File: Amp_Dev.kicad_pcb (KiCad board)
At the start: 2 copper layers, 100 x 100 mm, 512 parts, among them J1 SMA, J10 SMA, J11 CONN_01X02, J12 TEST_1P, J13 SMA, J14 CONN_01X02, J15 CONN_01X03, J16 TEST_1P, J17 TEST_1P, J18 TEST_1P, J2 SMA, J20 SMA, J21 SMA, J22 SMA, J3 TEST_1P, J4 TEST_1P, J5 CONN_01X03, J6 TEST_1P, J7 CONN_01X03, J8 TEST_1P, J9 TEST_1P, Q1 DMN2075U, U1 MML09211H, U2 RF6886, U3 LMV358, U4 SN74LVC1G17, U5 TLV702, U6 LTC2644, U7 RT9183

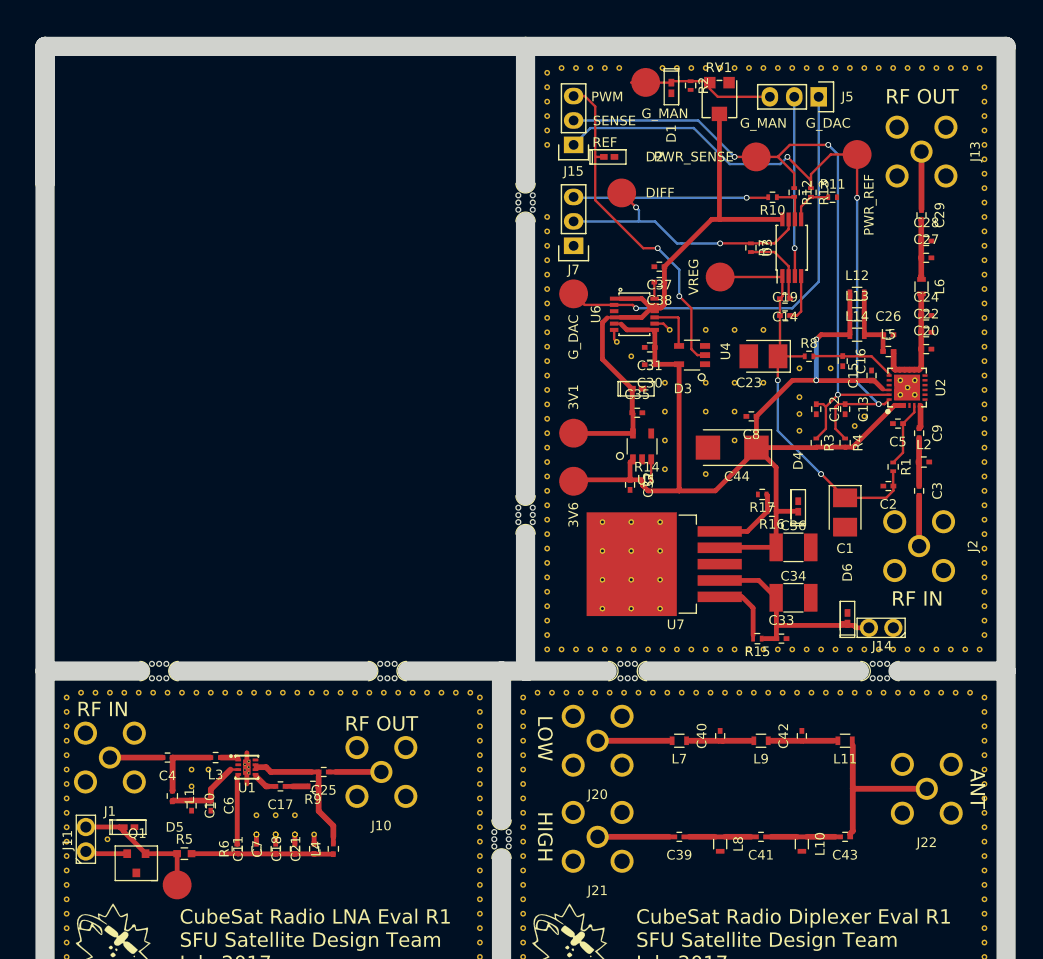
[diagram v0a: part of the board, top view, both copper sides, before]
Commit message: placed reference designators. resolves #9
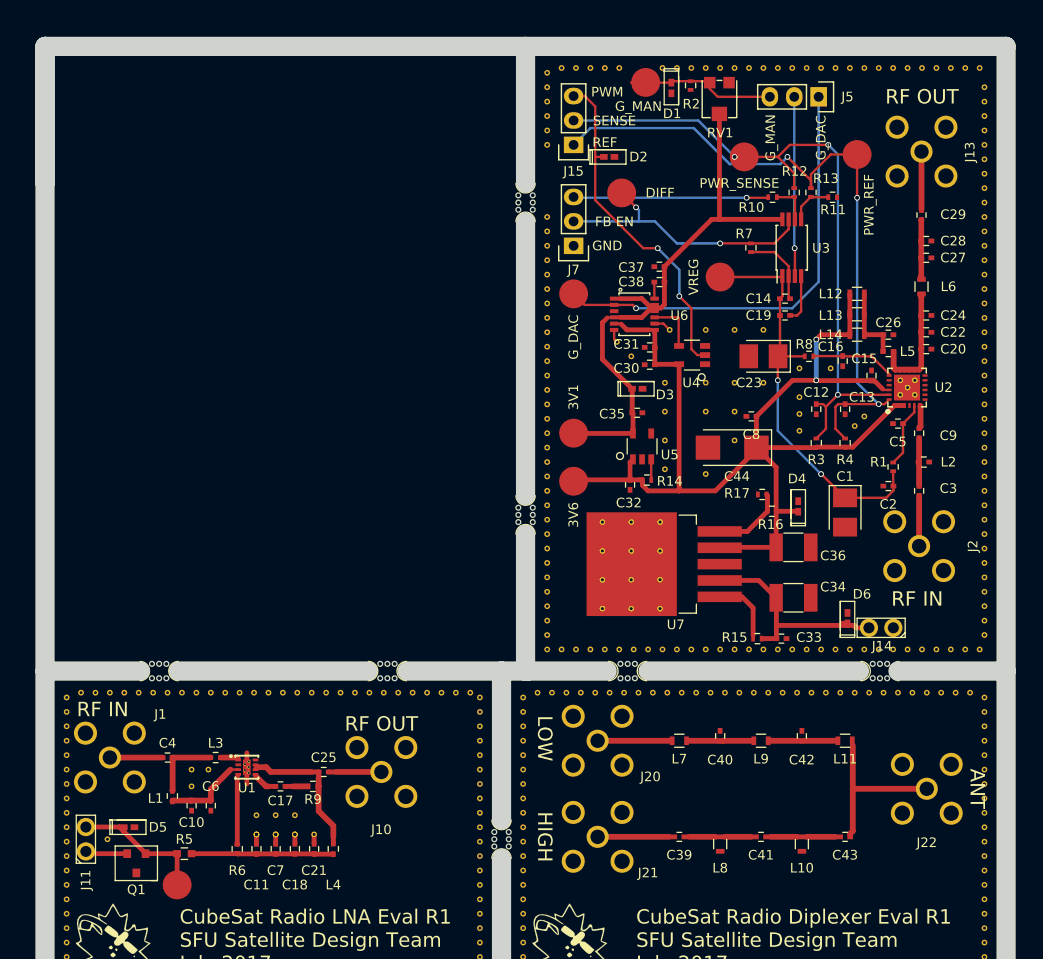
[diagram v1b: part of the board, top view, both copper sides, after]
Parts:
- moved J8 1.25 mm to (172.8, 61.5)
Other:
- board text added: "FB EN"
- board text added: "GND"

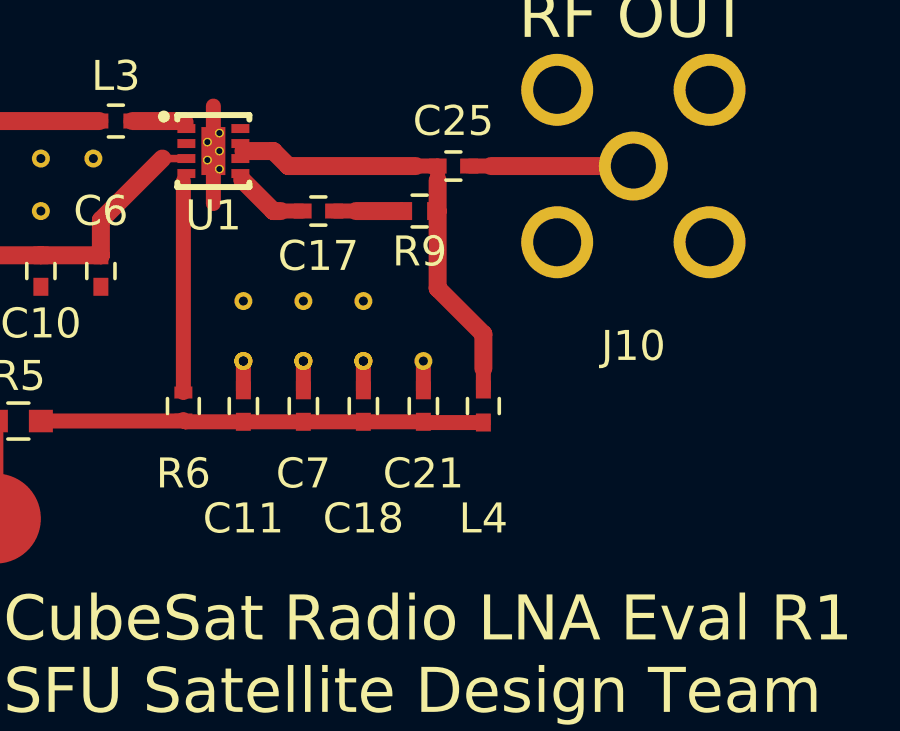
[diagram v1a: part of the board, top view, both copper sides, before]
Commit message: moved L4 closer to RF trace
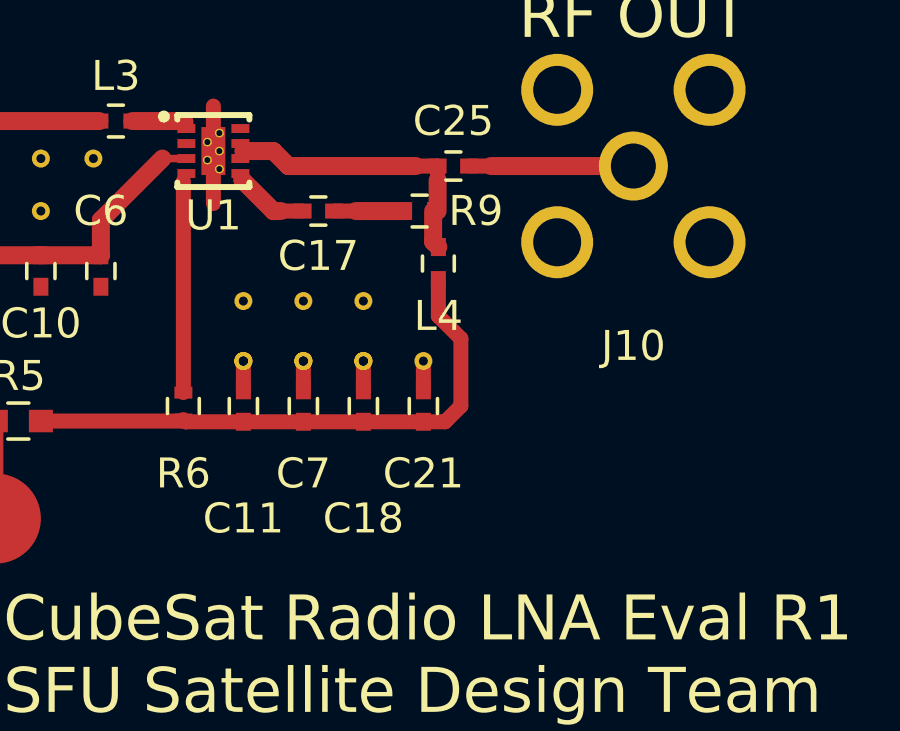
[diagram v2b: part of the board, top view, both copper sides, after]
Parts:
- moved L4 4.98 mm to (128.5, 128.8)
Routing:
- net Net-(C25-Pad2): track 15.3 -> 9.99 mm
- net Net-(C11-Pad1): track 14.9 -> 18.9 mm
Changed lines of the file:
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@@
     (links 631)
     (no_connects 2)
-    (area 98.999999 48.999999 201.000001 151.000001)
+    (area -1.420237 -0.9 202.188095 159.700001)
     (thickness 0.6)
     (drawings 44)
-    (tracks 454)
+    (tracks 456)
     (zones 0)
     (modules 512)
@@
     (tags "resistor 0402")
     (attr smd)
-    (fp_text reference R9 (at 0 -1.35 180) (layer F.SilkS)
+    (fp_text reference R9 (at -1.875 0 180) (layer F.SilkS)
       (effects (font (size 1 1) (thickness 0.15)))
     )
@@
   )
   (module SFUSat:L_0402 (layer F.Cu)
-    (at 130 133.5 90)
+    (at 128.5 128.75 90)
     (descr "Resistor SMD 0402, reflow soldering, Vishay (see dcrcw.pdf)")
     (tags "resistor 0402")
     (attr smd)
-    (fp_text reference L4 (at -3.75 0 180) (layer F.SilkS)
+    (fp_text reference L4 (at -1.75 0 180) (layer F.SilkS)
       (effects (font (size 1 1) (thickness 0.15)))
     )
@@
   (segment (start 124 132) (end 124 132.975) (width 0.5) (layer F.Cu) (net 4))
   (segment (start 122 132) (end 122 132.975) (width 0.5) (layer F.Cu) (net 4))
+  (segment (start 128.5 129.3) (end 128.5 130.5) (width 0.5) (layer F.Cu) (net 5) (status 400000))
+  (segment (start 128.725 134.025) (end 128 134.025) (width 0.5) (layer F.Cu) (net 5) (status 800000))
+  (segment (start 129.25 133.5) (end 128.725 134.025) (width 0.5) (layer F.Cu) (net 5))
+  (segment (start 129.25 131.25) (end 129.25 133.5) (width 0.5) (layer F.Cu) (net 5))
+  (segment (start 128.5 130.5) (end 129.25 131.25) (width 0.5) (layer F.Cu) (net 5))
   (segment (start 122 134.025) (end 120.075 134.025) (width 0.5) (layer F.Cu) (net 5))
   (segment (start 120.075 134.025) (end 120 133.95) (width 0.5) (layer F.Cu) (net 5))
@@
   (segment (start 126 134.025) (end 124 134.025) (width 0.5) (layer F.Cu) (net 5))
   (segment (start 128 134.025) (end 126 134.025) (width 0.5) (layer F.Cu) (net 5))
-  (segment (start 130 134.05) (end 128.025 134.05) (width 0.5) (layer F.Cu) (net 5))
   (segment (start 128.025 134.05) (end 128 134.025) (width 0.5) (layer F.Cu) (net 5))
   (segment (start 122.025 134.05) (end 122 134.025) (width 0.5) (layer F.Cu) (net 5))
@@
   (segment (start 135 125.5) (end 130.25 125.5) (width 0.6) (layer F.Cu) (net 8))
   (segment (start 130.25 125.5) (end 129.525 125.5) (width 0.5) (layer F.Cu) (net 8))
+  (segment (start 128.325 127) (end 128.325 128.025) (width 0.6) (layer F.Cu) (net 9) (status C00000))
+  (segment (start 128.325 128.025) (end 128.5 128.2) (width 0.6) (layer F.Cu) (net 9) (status C00000))
   (segment (start 128.475 125.975) (end 128.475 127) (width 0.6) (layer F.Cu) (net 9))
   (segment (start 128.475 125.5) (end 128.475 125.975) (width 0.5) (layer F.Cu) (net 9))
   (segment (start 128.475 125.975) (end 128.5 126) (width 0.5) (layer F.Cu) (net 9))
-  (segment (start 130 132.25) (end 130 131.1) (width 0.6) (layer F.Cu) (net 9))
-  (segment (start 130 131.1) (end 128.475 129.575) (width 0.6) (layer F.Cu) (net 9))
-  (segment (start 128.475 127) (end 128.475 129.575) (width 0.6) (layer F.Cu) (net 9))
-  (segment (start 130 132.25) (end 130 132.95) (width 0.5) (layer F.Cu) (net 9))
   (segment (start 128.475 125.5) (end 127.75 125.5) (width 0.5) (layer F.Cu) (net 9))
   (segment (start 123 125) (end 122 125) (width 0.6) (layer F.Cu) (net 9))

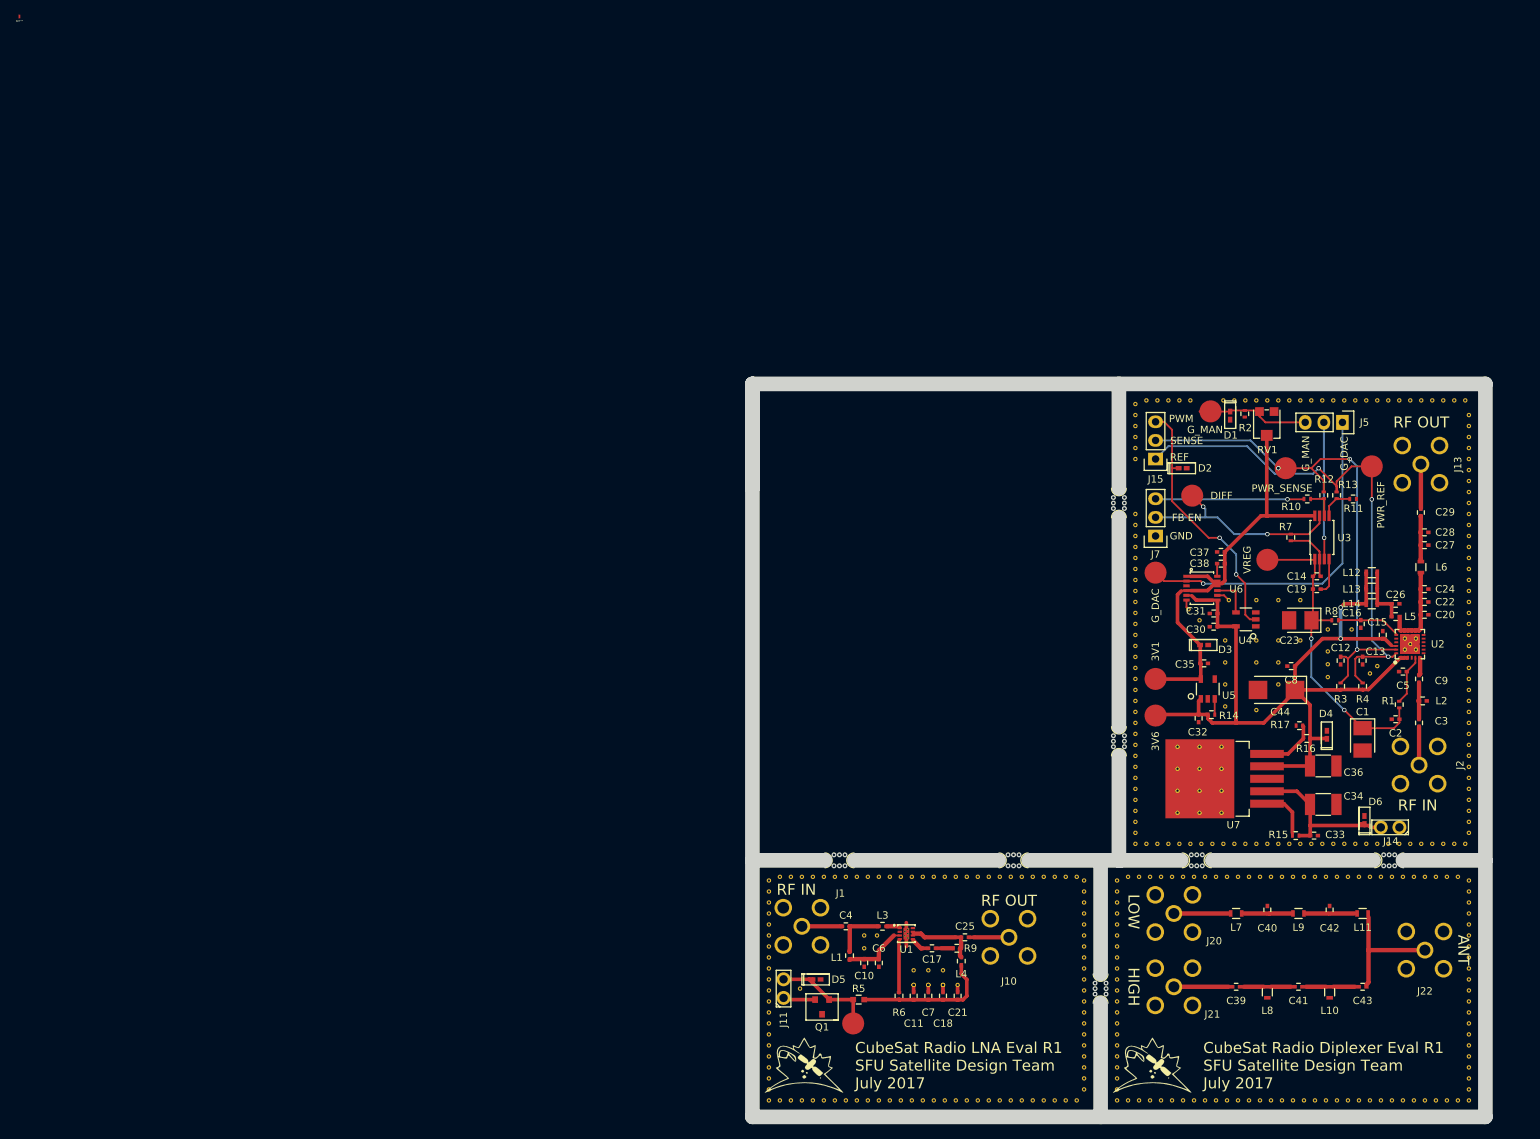
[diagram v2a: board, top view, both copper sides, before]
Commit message: made text thinner
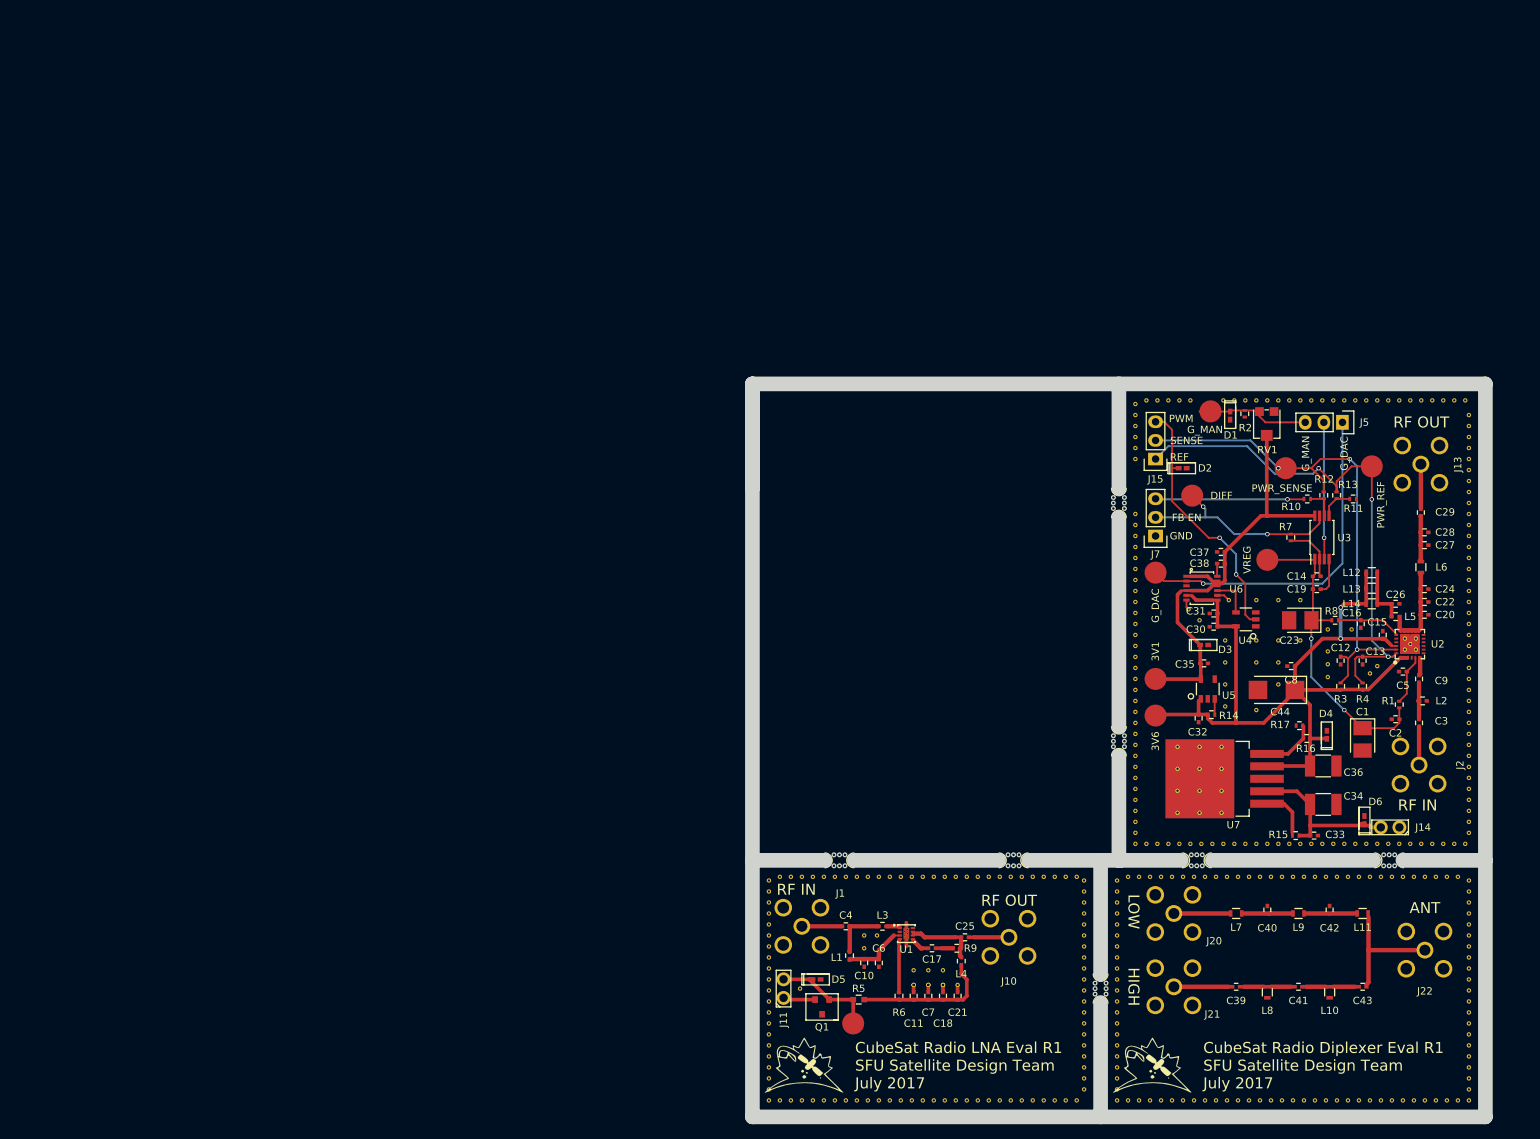
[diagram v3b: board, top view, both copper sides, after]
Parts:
- removed the REF** at (0.00, 0.00)
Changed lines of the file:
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@@
     (tracks 456)
     (zones 0)
-    (modules 512)
+    (modules 511)
     (nets 64)
   )
@@
     (add_net "Net-(L3-Pad1)")
   )
-  (module muwave_stub (layer F.Cu)
-    (at 0 0)
-    (fp_text reference REF** (at 0 0.5) (layer F.SilkS)
-      (effects (font (size 0.25 0.25) (thickness 0.05)))
-    )
-    (fp_text value muwave_stub (at 0 -0.5) (layer F.Fab)
-      (effects (font (size 0.25 0.25) (thickness 0.05)))
-    )
-    (pad 1 smd rect (at 0 0) (size 0.25 0.25) (layers F.Cu))
-    (pad 1 smd rect (at 0 -0.25) (size 0.25 0.25) (layers F.Cu))
-  )
   (module SFUSat:CP_Tantalum_Case-B_EIA-1411-21_Reflow (layer F.Cu)
     (at 183.25 98.5 270)
@@
   (module SFUSat:2x01In_Header_v2 (layer F.Cu)
     (at 187 110.5 180)
-    (fp_text reference J14 (at -0.1 -1.9 180) (layer F.SilkS)
+    (fp_text reference J14 (at -4.5 0 180) (layer F.SilkS)
       (effects (font (size 1 1) (thickness 0.15)))
     )
@@
   (gr_line (start 100 64.25) (end 100 50) (angle 90) (layer Edge.Cuts) (width 2))
   (gr_text "CubeSat Radio PA Eval R1 \nSFU Satellite Design Team\nJuly 2017" (at 157.75 98.75 270) (layer B.SilkS)
-    (effects (font (size 1.5 1.5) (thickness 0.3)) (justify left mirror))
+    (effects (font (size 1.5 1.5) (thickness 0.2)) (justify left mirror))
   )
   (gr_text PWR_REF (at 185.75 66.5 90) (layer F.SilkS)
@@
   )
   (gr_text "RF OUT" (at 191.25 55.25) (layer F.SilkS)
-    (effects (font (size 1.5 1.5) (thickness 0.3)))
+    (effects (font (size 1.5 1.5) (thickness 0.2)))
   )
   (gr_text "RF IN" (at 190.75 107.5) (layer F.SilkS)
-    (effects (font (size 1.5 1.5) (thickness 0.3)))
+    (effects (font (size 1.5 1.5) (thickness 0.2)))
   )
   (gr_line (start 150 100.75) (end 150 115) (angle 90) (layer Edge.Cuts) (width 2))
@@
   (gr_line (start 147.5 115) (end 158.5 115) (angle 90) (layer Edge.Cuts) (width 2))
   (gr_text HIGH (at 152 132.25 270) (layer F.SilkS)
-    (effects (font (size 1.5 1.5) (thickness 0.3)))
+    (effects (font (size 1.5 1.5) (thickness 0.2)))
   )
   (gr_text LOW (at 152 122 270) (layer F.SilkS)
-    (effects (font (size 1.5 1.5) (thickness 0.3)))
+    (effects (font (size 1.5 1.5) (thickness 0.2)))
   )
-  (gr_text ANT (at 197 127.25 270) (layer F.SilkS)
-    (effects (font (size 1.5 1.5) (thickness 0.3)))
+  (gr_text ANT (at 191.75 121.5) (layer F.SilkS)
+    (effects (font (size 1.5 1.5) (thickness 0.2)))
   )
   (gr_line (start 137.7 115) (end 147.5 115) (angle 90) (layer Edge.Cuts) (width 2))
@@
   (gr_line (start 147.5 134.5) (end 147.5 150) (angle 90) (layer Edge.Cuts) (width 2))
   (gr_text "CubeSat Radio Diplexer Eval R1 \nSFU Satellite Design Team\nJuly 2017" (at 161.5 143) (layer F.SilkS)
-    (effects (font (size 1.5 1.5) (thickness 0.3)) (justify left))
+    (effects (font (size 1.5 1.5) (thickness 0.2)) (justify left))
   )
   (gr_text "CubeSat Radio LNA Eval R1 \nSFU Satellite Design Team\nJuly 2017" (at 114 143) (layer F.SilkS)
-    (effects (font (size 1.5 1.5) (thickness 0.3)) (justify left))
+    (effects (font (size 1.5 1.5) (thickness 0.2)) (justify left))
   )
   (gr_text "RF OUT" (at 135 120.5) (layer F.SilkS)
-    (effects (font (size 1.5 1.5) (thickness 0.3)))
+    (effects (font (size 1.5 1.5) (thickness 0.2)))
   )
   (gr_text "RF IN" (at 106 119) (layer F.SilkS)
-    (effects (font (size 1.5 1.5) (thickness 0.3)))
+    (effects (font (size 1.5 1.5) (thickness 0.2)))
   )
   (dimension 100 (width 0.3) (layer F.Fab)
@@
   (segment (start 124 132) (end 124 132.975) (width 0.5) (layer F.Cu) (net 4))
   (segment (start 122 132) (end 122 132.975) (width 0.5) (layer F.Cu) (net 4))
-  (segment (start 128.5 129.3) (end 128.5 130.5) (width 0.5) (layer F.Cu) (net 5) (status 400000))
-  (segment (start 128.725 134.025) (end 128 134.025) (width 0.5) (layer F.Cu) (net 5) (status 800000))
+  (segment (start 128.5 129.3) (end 128.5 130.5) (width 0.5) (layer F.Cu) (net 5))
+  (segment (start 128.725 134.025) (end 128 134.025) (width 0.5) (layer F.Cu) (net 5))
   (segment (start 129.25 133.5) (end 128.725 134.025) (width 0.5) (layer F.Cu) (net 5))
   (segment (start 129.25 131.25) (end 129.25 133.5) (width 0.5) (layer F.Cu) (net 5))
@@
   (segment (start 135 125.5) (end 130.25 125.5) (width 0.6) (layer F.Cu) (net 8))
   (segment (start 130.25 125.5) (end 129.525 125.5) (width 0.5) (layer F.Cu) (net 8))
-  (segment (start 128.325 127) (end 128.325 128.025) (width 0.6) (layer F.Cu) (net 9) (status C00000))
-  (segment (start 128.325 128.025) (end 128.5 128.2) (width 0.6) (layer F.Cu) (net 9) (status C00000))
+  (segment (start 128.325 127) (end 128.325 128.025) (width 0.6) (layer F.Cu) (net 9))
+  (segment (start 128.325 128.025) (end 128.5 128.2) (width 0.6) (layer F.Cu) (net 9))
   (segment (start 128.475 125.975) (end 128.475 127) (width 0.6) (layer F.Cu) (net 9))
   (segment (start 128.475 125.5) (end 128.475 125.975) (width 0.5) (layer F.Cu) (net 9))
